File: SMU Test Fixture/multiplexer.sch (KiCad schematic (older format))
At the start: 3 parts, among them J1 AD2 Connector, J2 AD2 Connector, K1 External Source Enable

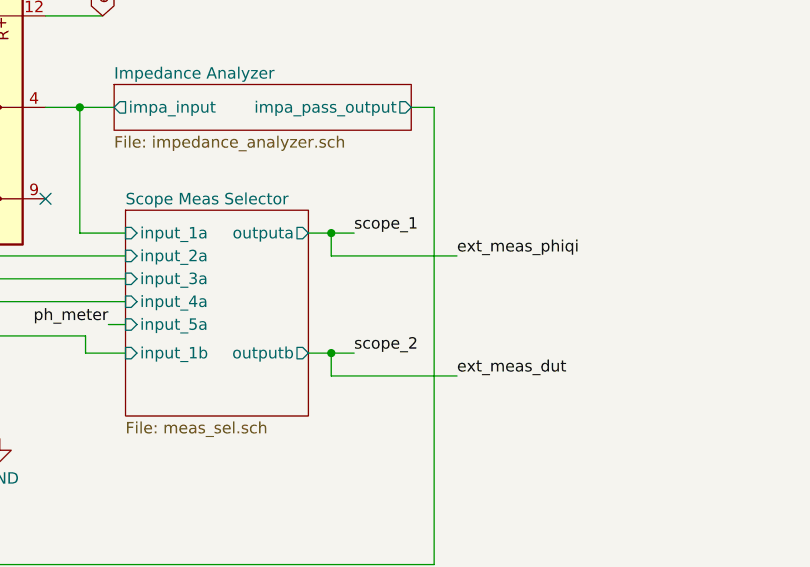
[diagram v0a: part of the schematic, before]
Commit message: Add simulations and relay state spreadsheet
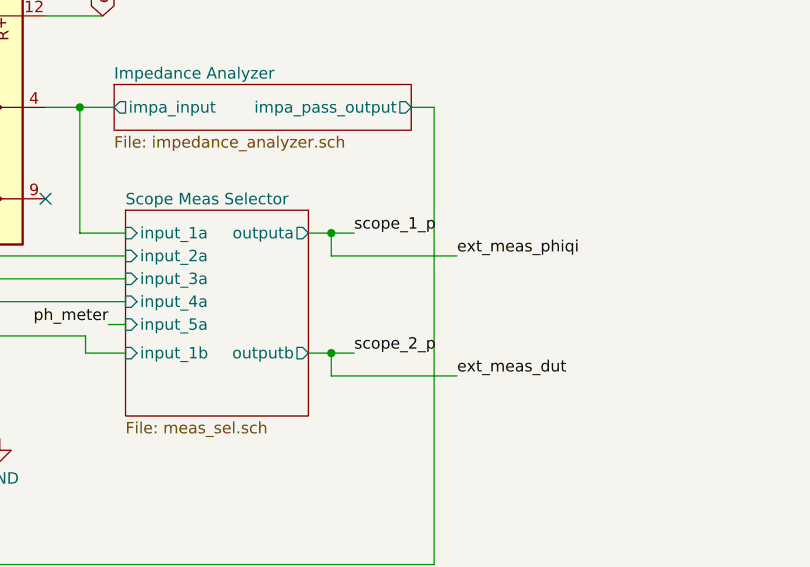
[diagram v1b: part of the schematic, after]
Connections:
- net scope_1_p is gone; now on net ext_meas_phiqi: J1.29 (Pin_29)
- net scope_2_p is gone; now on net ext_meas_dut: J1.27 (Pin_27)
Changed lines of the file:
@@
 Connection ~ 3425 4650
 Text Label 6175 4725 0    50   ~ 0
-scope_2
+scope_2_p
 Text Label 6175 4200 0    50   ~ 0
-scope_1
+scope_1_p
 Wire Wire Line
 	6175 4200 6075 4200

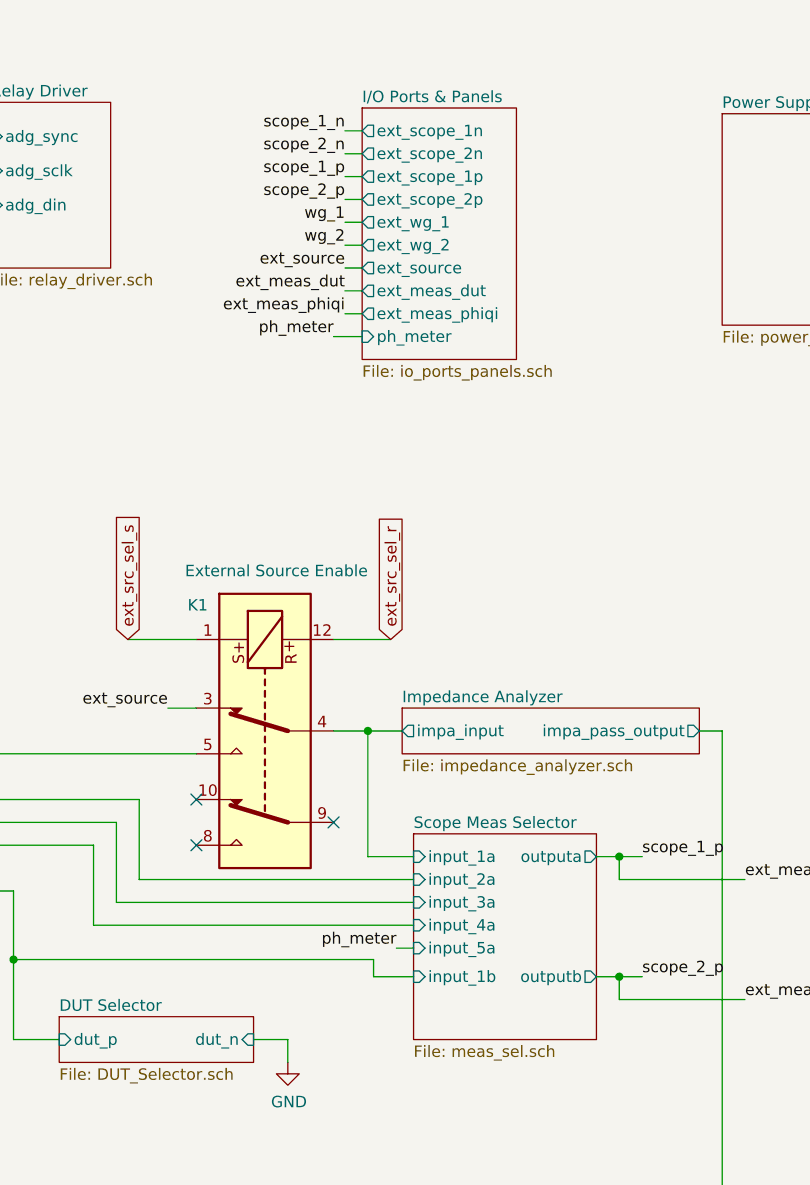
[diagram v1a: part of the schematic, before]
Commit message: Elminate extra scope cal relay, re-organize relays, re-annotate, ERC
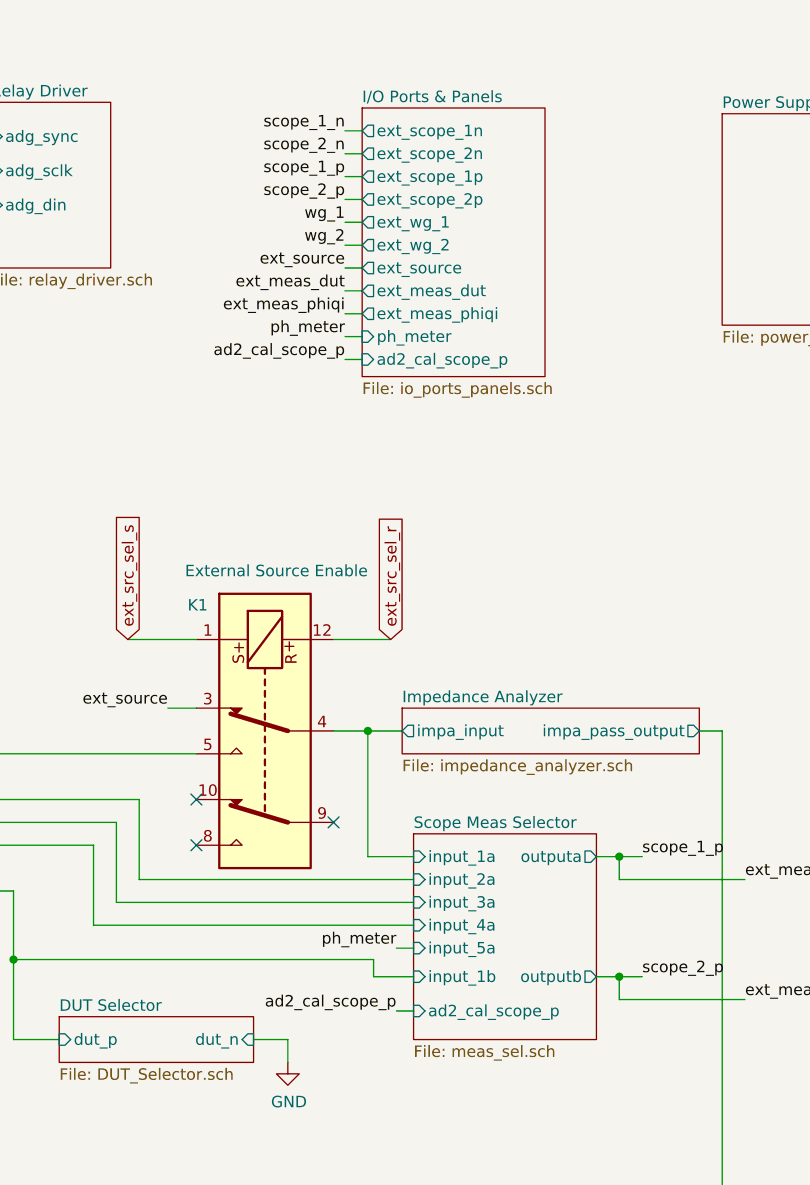
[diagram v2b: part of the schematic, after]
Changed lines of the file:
@@
 F8 "phi_int_output" O R 3275 3950 50
-$EndSheet
-$Sheet
-S 3625 4900 850  200
-U 600C9795
-F0 "DUT Selector" 50
-F1 "DUT_Selector.sch" 50
-F2 "dut_p" I L 3625 5000 50
-F3 "dut_n" I R 4475 5000 50
 $EndSheet
 $Comp
@@
 	4625 5000 4475 5000
 $Sheet
-S 4950 925  675  1100
+S 4950 925  800  1175
 U 5FC2AF5A
 F0 "I/O Ports & Panels" 50
@@
 F10 "ext_meas_phiqi" O L 4950 1825 50
 F11 "ph_meter" I L 4950 1925 50
+F12 "ad2_cal_scope_p" I L 4950 2025 50
 $EndSheet
 $Comp
@@
 Wire Wire Line
 	5100 4600 5175 4600
-Text Label 4825 1925 2    50   ~ 0
+Text Label 4875 1925 2    50   ~ 0
 ph_meter
 Wire Wire Line
-	4825 1925 4950 1925
+	4875 1925 4950 1925
 Wire Wire Line
 	5000 4650 5000 4725
@@
 F8 "outputb" O R 5975 4725 50
 F9 "input_1b" I L 5175 4725 50
+F10 "ad2_cal_scope_p" I L 5175 4875 50
 $EndSheet
 Wire Wire Line
@@
 F1 "power_supplies.sch" 50
 $EndSheet
+$Sheet
+S 3625 4900 850  200
+U 600C9795
+F0 "DUT Selector" 50
+F1 "DUT_Selector.sch" 50
+F2 "dut_p" I L 3625 5000 50
+F3 "dut_n" I R 4475 5000 50
+$EndSheet
+Text Label 4875 2025 2    50   ~ 0
+ad2_cal_scope_p
+Wire Wire Line
+	4875 2025 4950 2025
+Text Label 5100 4875 2    50   ~ 0
+ad2_cal_scope_p
+Wire Wire Line
+	5100 4875 5175 4875
 $EndSCHEMATC

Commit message: Footprint updates
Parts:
- J1, J2: footprint (none) -> Connector_PinHeader_2.54mm:PinHeader_2x15_P2.54mm_Horizontal; PN (none) -> PPPC152LJBN-RC
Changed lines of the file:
@@
 F 0 "J1" H 1450 2417 50  0000 C CNN
 F 1 "AD2 Connector" H 1450 2326 50  0000 C CNN
-F 2 "" H 1400 1500 50  0001 C CNN
+F 2 "Connector_PinHeader_2.54mm:PinHeader_2x15_P2.54mm_Horizontal" H 1400 1500 50  0001 C CNN
 F 3 "~" H 1400 1500 50  0001 C CNN
+F 4 "PPPC152LJBN-RC" H 1400 1500 50  0001 C CNN "PN"
+F 5 "" H 1400 1500 50  0001 C CNN "Field5"
 	1    1400 1500
 	1    0    0    -1
@@
 F 0 "J2" H 9450 2542 50  0000 C CNN
 F 1 "AD2 Connector" H 9450 2451 50  0000 C CNN
-F 2 "" H 9400 1625 50  0001 C CNN
+F 2 "Connector_PinHeader_2.54mm:PinHeader_2x15_P2.54mm_Horizontal" H 9400 1625 50  0001 C CNN
 F 3 "~" H 9400 1625 50  0001 C CNN
+F 4 "PPPC152LJBN-RC" H 9400 1625 50  0001 C CNN "PN"
 	1    9400 1625
 	1    0    0    -1
